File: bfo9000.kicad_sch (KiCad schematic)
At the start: 122 parts, among them U1 ProMicro, U2 TRRS, U3 TRRS

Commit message: Replace reset button with SMD one
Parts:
- R1, R2: footprint Keebio-Parts:Resistor-Compact-1-side -> Keebio-Parts:R_0603
- SW_A1, SW_A2, SW_A3, SW_A4, SW_A5, SW_A6, SW_A7, SW_A8, SW_A9, SW_B1, SW_B2, SW_B3, SW_B4, SW_B5, SW_B6, SW_B7, SW_B8, SW_B9, SW_C1, SW_C2, SW_C3, SW_C4, SW_C5, SW_C6, SW_C7, SW_C8, SW_C9, SW_D1, SW_D2, SW_D3, SW_D4, SW_D5, SW_D6, SW_D7, SW_D8, SW_D9, SW_E1, SW_E2, SW_E3, SW_E4, SW_E5, SW_E6, SW_E7, SW_E8, SW_E9, SW_F1, SW_F2, SW_F3, SW_F4, SW_F5, SW_F6, SW_F7, SW_F8, SW_F9: footprint Keebio-Parts:MX-Alps-Choc-1U-NoLED -> Keebio-Parts:MX-Alps-Choc-1U-NoLED-Alt
- SW_RESET1: footprint Keebio-Parts:SW_Tactile_SPST_Angled_MJTP1117 -> Keebio-Parts:SW_SPST_TL3342
- U1: footprint Keebio-Parts:ArduinoProMicro -> Keebio-Parts:ArduinoProMicro-ZigZag

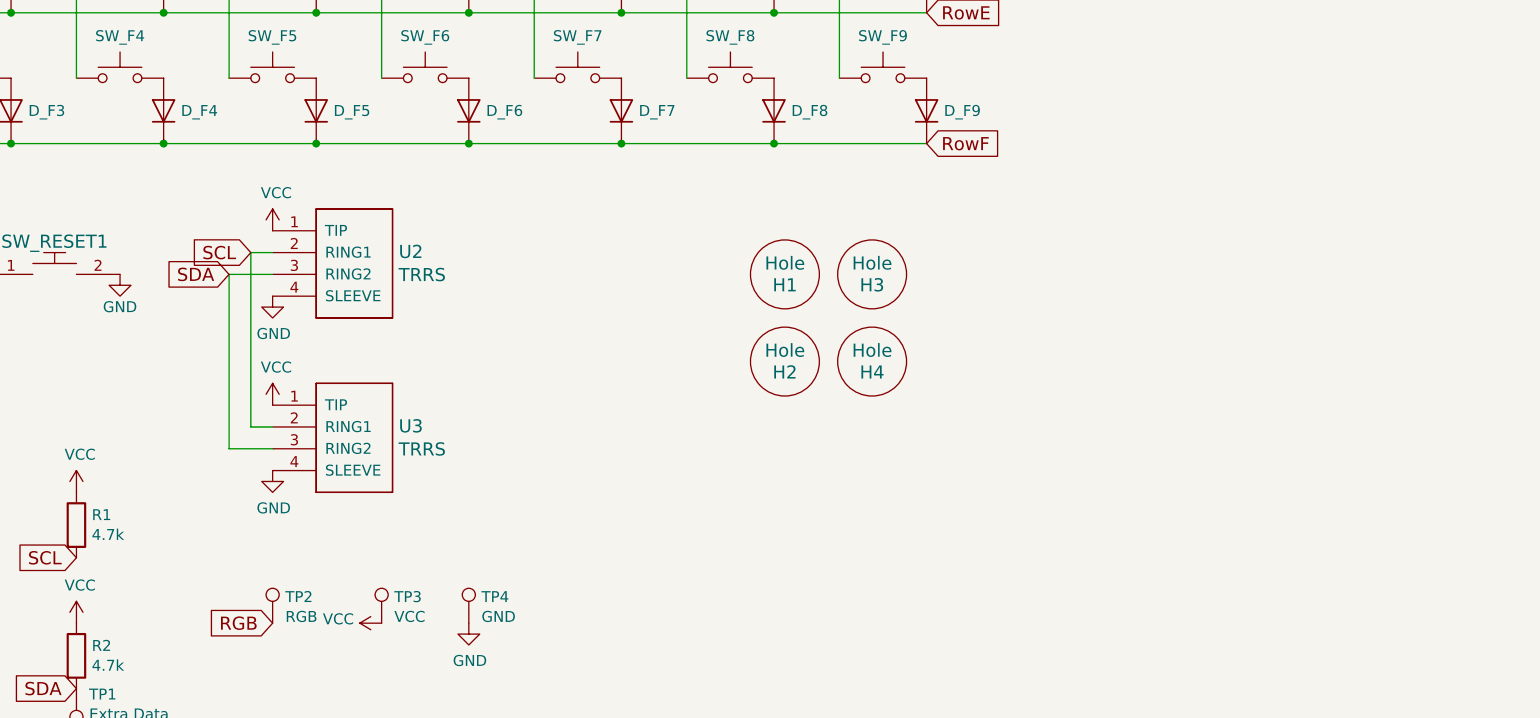
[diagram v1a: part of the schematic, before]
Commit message: Replace TRRS with USB-C
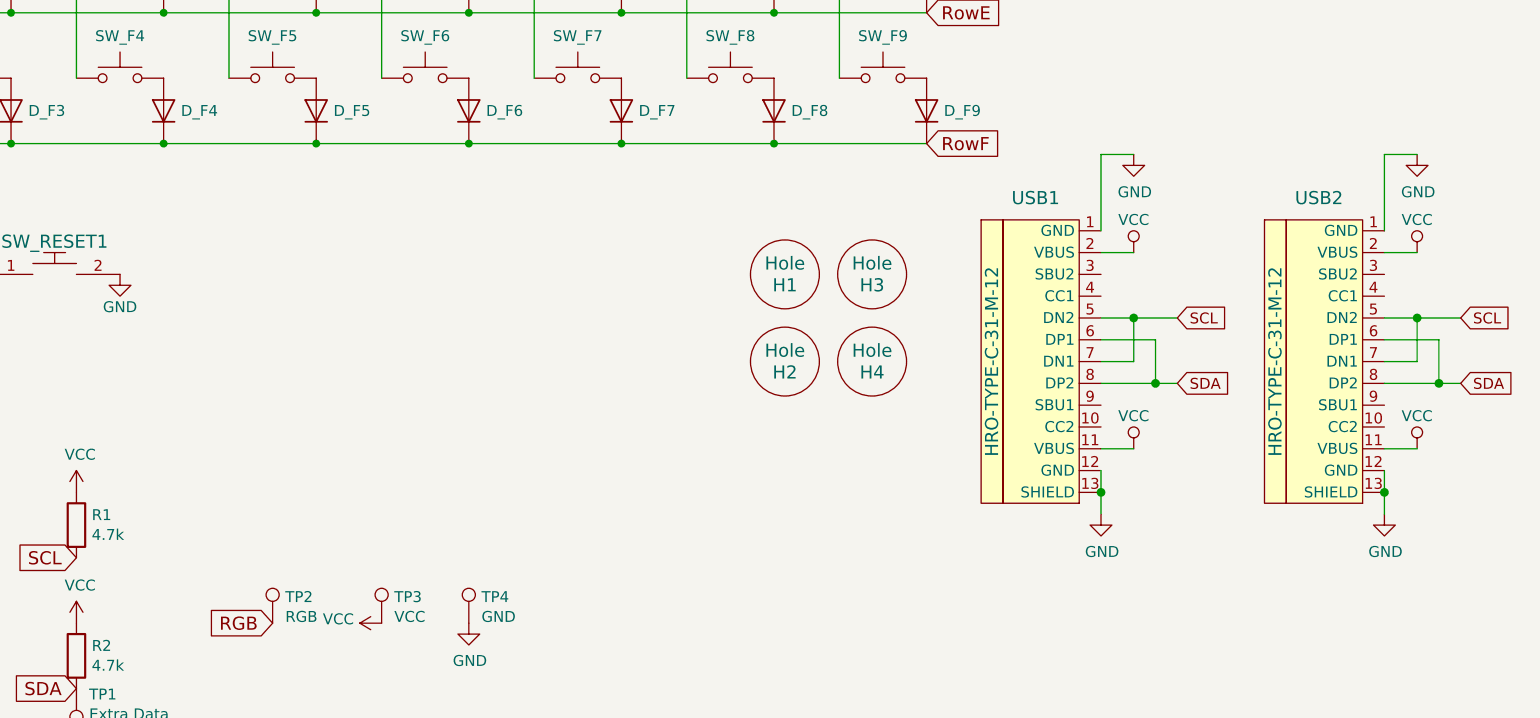
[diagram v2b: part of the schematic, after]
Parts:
- removed U2, U3: TRRS, Keebio-Parts:TRRS-PJ-320A, symbol bfo9000-rescue:TRRS-keebio
- added USB1, USB2: HRO-TYPE-C-31-M-12, Keebio-Parts:HRO-TYPE-C-31-M-12-Assembly, symbol keebio:HRO-TYPE-C-31-M-12
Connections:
- net GND: now also USB1.1 (GND), USB1.12 (GND), USB1.13 (SHIELD), USB2.1 (GND), USB2.12 (GND), USB2.13 (SHIELD)
- net SCL: now also USB1.5 (DN2), USB1.7 (DN1), USB2.5 (DN2), USB2.7 (DN1)
- net SDA: now also USB1.6 (DP1), USB1.8 (DP2), USB2.6 (DP1), USB2.8 (DP2)
- net VCC: now also USB1.11 (VBUS), USB1.2 (VBUS), USB2.11 (VBUS), USB2.2 (VBUS)

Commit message: Add KS-33 and Choc V2 support
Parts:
- SW_A1, SW_A2, SW_A3, SW_A4, SW_A5, SW_A6, SW_A7, SW_A8, SW_A9, SW_B1, SW_B2, SW_B3, SW_B4, SW_B5, SW_B6, SW_B7, SW_B8, SW_B9, SW_C1, SW_C2, SW_C3, SW_C4, SW_C5, SW_C6, SW_C7, SW_C8, SW_C9, SW_D1, SW_D2, SW_D3, SW_D4, SW_D5, SW_D6, SW_D7, SW_D8, SW_D9, SW_E1, SW_E2, SW_E3, SW_E4, SW_E5, SW_E6, SW_E7, SW_E8, SW_E9, SW_F1, SW_F2, SW_F3, SW_F4, SW_F5, SW_F6, SW_F7, SW_F8, SW_F9: footprint Keebio-Parts:MX-Alps-Choc-1U-NoLED-Alt -> Keebio-Parts:MX-Alps-Choc_V1V2_KS-33-1U-NoLED-Alt
